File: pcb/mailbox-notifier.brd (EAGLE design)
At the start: 35 x 100 mm, 70 parts, among them CON1 3P-SH-SIDE, Q1 AO3401, U1 MCP73832, U10 MIC2019, U11 74LVC1G17, U2 MIC23155, U3 FS312F-G, U4 FS8205, U5 EFM32PG1B200F256GM32, U6 SST26VF016B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

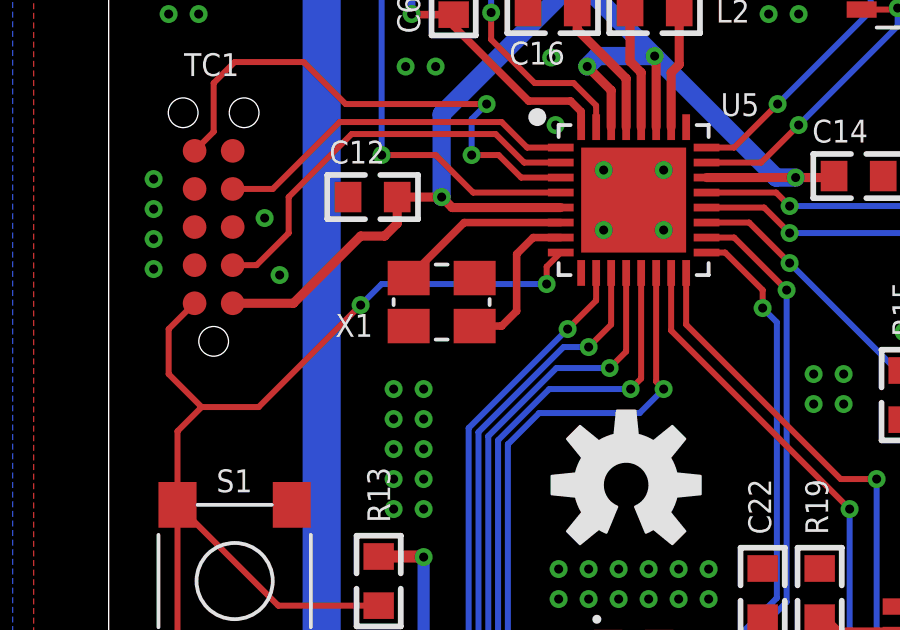
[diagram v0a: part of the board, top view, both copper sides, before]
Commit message: Change DRCs Change crystal package
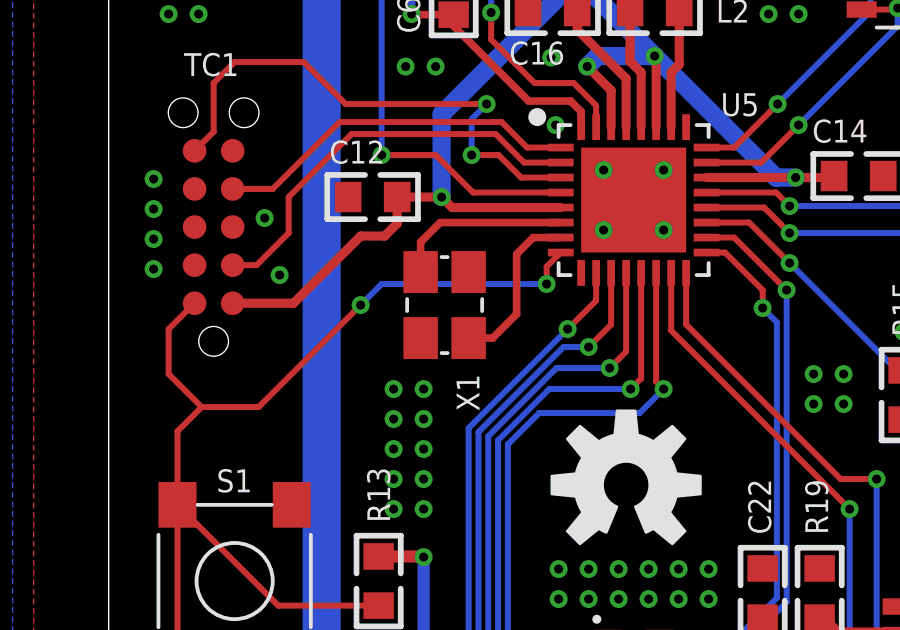
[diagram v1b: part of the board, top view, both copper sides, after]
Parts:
- U7: device HopeRF:RFM69W-XXXS2 -> HopeRF:RFM69XW-XXXS2
- moved X1 0.14 mm to (11.2, 48.8), turned to 90 degrees
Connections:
- net GND: now also X1.1, X1.3; no longer X1.2, X1.4
- net N$16: now also X1.2; no longer X1.1
- net N$17: now also X1.4; no longer X1.3
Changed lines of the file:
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@@
 <param name="srMinRoundness" value="0mil"/>
 <param name="srMaxRoundness" value="0mil"/>
-<param name="slThermalIsolate" value="10mil"/>
+<param name="slThermalIsolate" value="5mil"/>
 <param name="slThermalsForVias" value="0"/>
 <param name="dpMaxLengthDifference" value="10mm"/>
@@
 <attribute name="NAME" x="20.4" y="55.1" size="0.762" layer="25" font="vector" ratio="10"/>
 </element>
-<element name="U7" library="HopeRF" package="RFM69W-XXXS2" value="RFM69HW" x="17.5" y="12" smashed="yes" rot="R180">
+<element name="U7" library="HopeRF" package="RFM69XW-XXXS2" value="RFM69HW" x="17.5" y="12" smashed="yes" rot="R180">
 <attribute name="NAME" x="8.828" y="21.262" size="0.762" layer="25" font="vector" ratio="10" rot="R180"/>
 </element>
@@
 <attribute name="VALUE" x="23.832" y="36.2536" size="0.762" layer="27" font="vector" ratio="10" rot="SR90"/>
 </element>
-<element name="X1" library="Crystal" package="4-SMD-3225" value="40MHz" x="11.1" y="48.9" smashed="yes">
-<attribute name="NAME" x="7.56" y="47.74" size="0.762" layer="25" font="vector" ratio="10"/>
+<element name="X1" library="Crystal" package="4-SMD-3225" value="40MHz" x="11.2" y="48.8" smashed="yes" rot="R90">
+<attribute name="NAME" x="12.36" y="45.26" size="0.762" layer="25" font="vector" ratio="10" rot="R90"/>
 </element>
 <element name="U10" library="Microchip" package="SOT23-6" value="MIC2019" x="26.5" y="59.6" smashed="yes">
@@
 <contactref element="D3" pad="2"/>
 <contactref element="C22" pad="2"/>
-<contactref element="X1" pad="2"/>
-<contactref element="X1" pad="4"/>
+<contactref element="X1" pad="1"/>
+<contactref element="X1" pad="3"/>
 <polygon width="0.2" layer="1">
 <vertex x="-2.5" y="102.3"/>
@@
 <signal name="N$16">
 <contactref element="U5" pad="6"/>
-<contactref element="X1" pad="1"/>
-<wire x1="15.07" y1="51.55" x2="11.85" y2="51.55" width="0.254" layer="1"/>
-<wire x1="11.85" y1="51.55" x2="10" y2="49.7" width="0.254" layer="1"/>
+<contactref element="X1" pad="2"/>
+<wire x1="10.4" y1="49.9" x2="10.4" y2="50.9" width="0.254" layer="1"/>
+<wire x1="10.4" y1="50.9" x2="11.05" y2="51.55" width="0.254" layer="1"/>
+<wire x1="11.05" y1="51.55" x2="15.07" y2="51.55" width="0.254" layer="1"/>
 </signal>
 <signal name="N$17">
 <contactref element="U5" pad="7"/>
-<contactref element="X1" pad="3"/>
-<wire x1="12.2" y1="48.1" x2="13.1" y2="48.1" width="0.254" layer="1"/>
-<wire x1="13.1" y1="48.1" x2="13.6" y2="48.6" width="0.254" layer="1"/>
-<wire x1="13.6" y1="48.6" x2="13.6" y2="50.5" width="0.254" layer="1"/>
+<contactref element="X1" pad="4"/>
+<wire x1="13.6" y1="48.5" x2="13.6" y2="50.5" width="0.254" layer="1"/>
 <wire x1="14.15" y1="51.05" x2="15.07" y2="51.05" width="0.254" layer="1"/>
 <wire x1="13.6" y1="50.5" x2="14.15" y2="51.05" width="0.254" layer="1"/>
+<wire x1="12.8" y1="47.7" x2="12" y2="47.7" width="0.254" layer="1"/>
+<wire x1="13.6" y1="48.5" x2="12.8" y2="47.7" width="0.254" layer="1"/>
 </signal>
 <signal name="N$2">
